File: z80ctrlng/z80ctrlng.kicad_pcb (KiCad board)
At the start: 2 copper layers, 99.8 x 49.9 mm, 46 parts, among them J1 BUS, J2 Micro_SD_Card_Det2, J3 UEXT, J4 SERIAL, J6 UPDI, Q1 BSS138, SW1 RESET, SW2 SW_DPDT_x2, SW3 SW_SP3T, SW4 SW_DIP_x06, SW5 SW_DPST, SW6 SW_DPST, U1 AVR128DB64x-xPT, U2 MIC5504-3.3YM5, U3 MCP7940N-xST, U5 74HCT574, U6 74HCT257, U7 AS6C4008-55PCN, Y1 32kHz

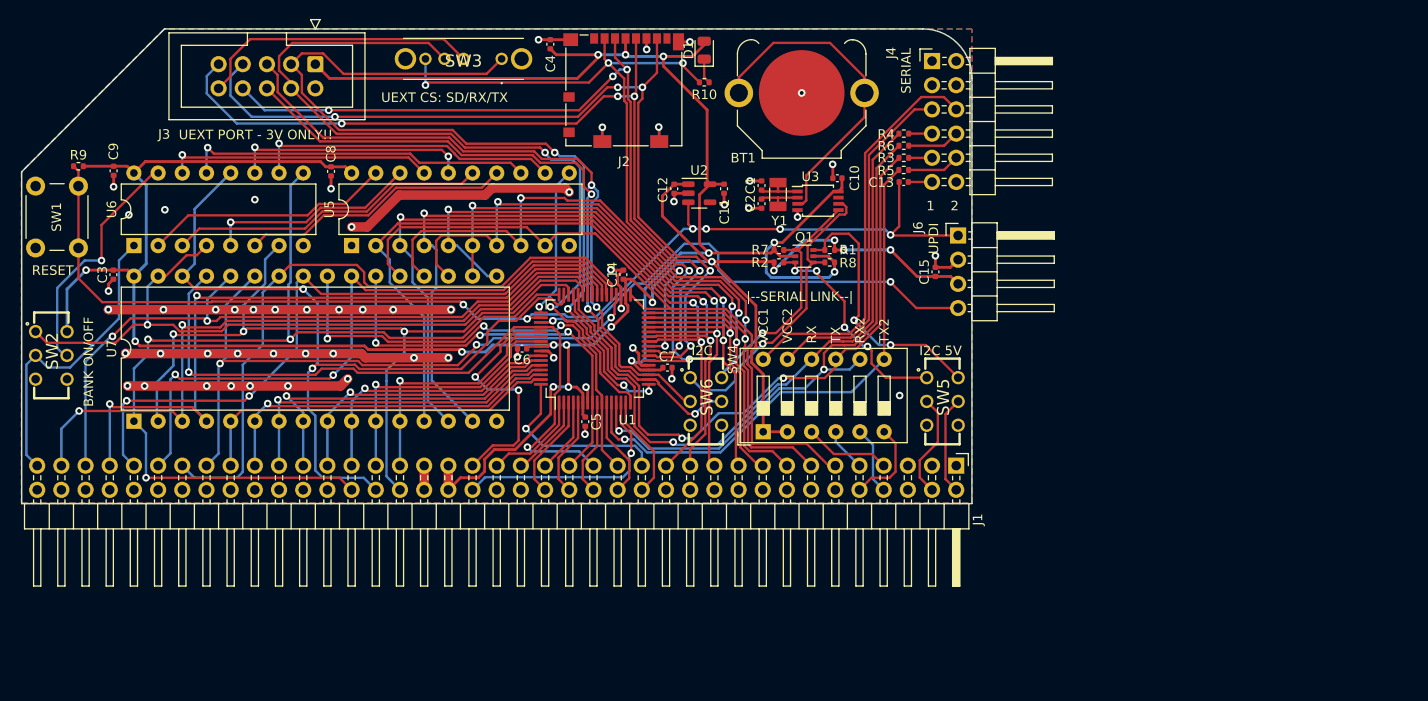
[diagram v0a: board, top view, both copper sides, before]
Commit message: Rework bus links using jumpers instead of dip switches; add labels
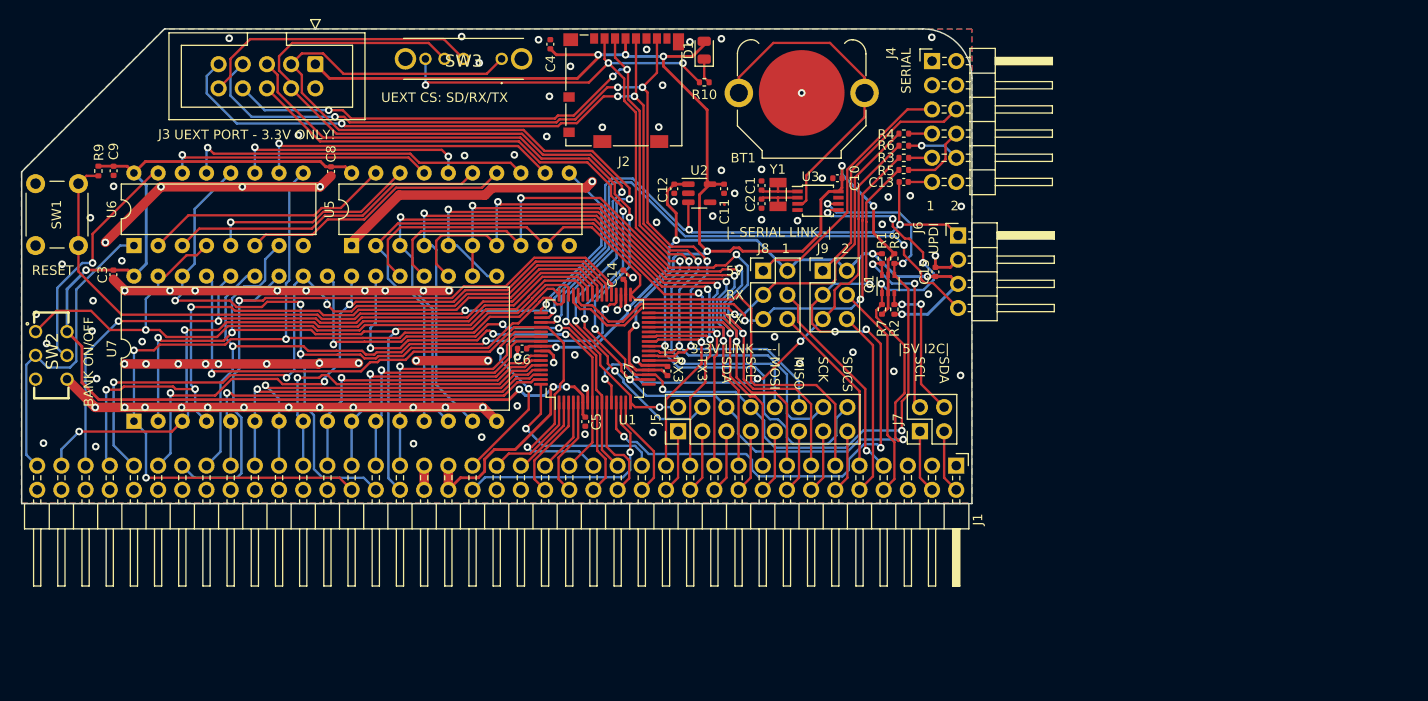
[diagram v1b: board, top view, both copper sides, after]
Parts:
- removed SW4: SW_DIP_x06, Button_Switch_THT:SW_DIP_SPSTx06_Slide_9.78x17.42mm_W7.62mm_P2.54mm
- removed SW5, SW6: SW_DPST, SamacSys_Parts:JS202011CQN
- added J5: 3V_LINK, Connector_PinHeader_2.54mm:PinHeader_2x08_P2.54mm_Vertical, F.Cu at (161.5, 100.5)
- added J7: I2C_LINK, Connector_PinHeader_2.54mm:PinHeader_2x02_P2.54mm_Vertical, F.Cu at (186.9, 100.5)
- added J8: S1_LINK, Connector_PinHeader_2.54mm:PinHeader_2x03_P2.54mm_Vertical, F.Cu at (170.5, 83.7)
- added J9: S2_LINK, Connector_PinHeader_2.54mm:PinHeader_2x03_P2.54mm_Vertical, F.Cu at (176.7, 83.7)
- moved R2 13.1 mm to (184.3, 87.7), turned to 90 degrees
- moved R7 12.5 mm to (183.0, 87.7), turned to 90 degrees
- moved Q1 9.27 mm to (183.6, 85.1), turned to 90 degrees
- moved R8 6.80 mm to (184.3, 82.4), turned to -90 degrees
- moved R1 5.56 mm to (183.0, 82.4), turned to -90 degrees
- moved R9 2.15 mm to (100.7, 73.2), turned to 90 degrees
- moved C7 0.36 mm to (160.4, 94.2), turned to 90 degrees
- moved SW1 0.25 mm to (94.1, 81.0)
- turned R6 to 180 degrees
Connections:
- J1 pad 43: +5V -> /5V
- J1 pad 44: +5V -> /5V
- Q1 pad 1: /SDA3V -> /SDA
- Q1 pad 3: /SCL5V -> /SDA5V
- Q1 pad 4: /SCL3V -> /SCL
- Q1 pad 6: /SDA5V -> /SCL5V
- R1 pad 2: /SDA5V -> /SCL5V
- R2 pad 2: /SCL5V -> /SDA5V
- R5 pad 1: /TX2 -> /RX2
- R5 pad 2: Net-(J4-Pin_10) -> Net-(J4-Pin_8)
- R6 pad 1: /RX2 -> Net-(J4-Pin_10)
- R6 pad 2: Net-(J4-Pin_8) -> /TX2
- R7 pad 2: /SDA3V -> /SDA
- R8 pad 2: /SCL3V -> /SCL
- U3 pad 5: /SDA3V -> /SDA
- U3 pad 6: /SCL3V -> /SCL
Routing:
- net /SDA: track 73.0 -> 142.3 mm, vias 3 -> 8
- net /SCL: track 71.4 -> 134.7 mm, vias 2 -> 6
- net /SCL3V: track 32.4 -> 0.00 mm, vias 1 -> 0
- net /~{SDCS}: track 71.9 -> 101.8 mm
- net GND: track 161.0 -> 187.9 mm, vias 57 -> 98
- net /SDA3V: track 25.6 -> 0.00 mm, vias 1 -> 0
- net /SCK: track 91.6 -> 113.0 mm
- net +5V: track 231.5 -> 212.3 mm, vias 14 -> 10
- net /RX: track 69.1 -> 50.0 mm
- net Net-(J4-Pin_6): track 42.4 -> 25.4 mm
- net /TX: track 66.6 -> 50.5 mm
- net /RX2: track 61.2 -> 77.2 mm, vias 2 -> 5
- net /BRX2: track 7.13 -> 23.0 mm
- net /MISO: track 93.0 -> 108.1 mm
- net /BTX: track 4.59 -> 18.5 mm
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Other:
- board text added: "512KB SRAM"
- board text added: "5V"
- board text added: "AVR128DB64"
- board text added: "BANK MULTIPLEXER"
- board text added: "BANK REGISTER"
- board text added: "GND"
- board text added: "MISO"
- board text added: "MOSI"
- board text added: "PA1"
- board text added: "PA2"
- board text added: "PA3"
- board text added: "PA4"
- board text added: "PA5^"
- board text added: "PA6"
- board text added: "PA7^"
- board text added: "PB0"
- board text added: "PB1^"
- board text added: "PB2"
- board text added: "PB3^"
- board text added: "PB4^"
- board text added: "PB5^"
- board text added: "PB6^"
- board text added: "PB7^"
- board text added: "PC0"
- board text added: "PC1"
- board text added: "PC2"
- board text added: "PC3"
- board text added: "PC4"
- board text added: "PC5"
- board text added: "PC6"
- board text added: "PC7"
- board text added: "PD0"
- board text added: "PD1"
- board text added: "PD2"
- board text added: "PD3"
- board text added: "PD4"
- board text added: "PD5"
- board text added: "PD6"
- board text added: "PD7"
- board text added: "PE0"
- board text added: "PE1"
- board text added: "PE2"
- board text added: "PE3"
- board text added: "PE4"
- board text added: "PE5"
- board text added: "PE6"
- board text added: "PE7"
- board text added: "PF0^"
- board text added: "PF1^"
- board text added: "PF2^"
- board text added: "PF3^"
- board text added: "PF4^"
- board text added: "PF5"
- board text added: "PG0"
- board text added: "PG1"
- board text added: "PG2"
- board text added: "PG3"
- board text added: "PG4"
- board text added: "PG5"
- board text added: "PG6"
- board text added: "PG7"
- board text added: "RX3"
- board text added: "SCK"
- board text added: "SCL"
- board text added: "SDA"
- board text added: "SDCS"
- board text added: "TX3"
- board text added: "UEXT PORT - 3.3V ONLY!"
- board text added: "|- SERIAL LINK -|"
- board text added: "|---- 3.3V LINK ----|"
- board text added: "|5V I2C|"
- board text removed: "I2C"
- board text removed: "I2C 5V"
- board text removed: "RX2"
- board text removed: "TX2"
- board text removed: "UEXT PORT - 3V ONLY!!"
- board text removed: "VCC1"
- board text removed: "VCC2"
- board text removed: "|--SERIAL LINK--|"

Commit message: More cleanup, fixing errors
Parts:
- added J10: QWIIC, Custom:JST_SM04B-SRSS-TB_LF__SN_, F.Cu at (97.6, 87.6)
- added R11: 100K, Resistor_SMD:R_0402_1005Metric, F.Cu at (147.4, 62.4)
- added R12: 100K, Resistor_SMD:R_0402_1005Metric, F.Cu at (147.4, 65.4)
- added R13: 100K, Resistor_SMD:R_0402_1005Metric, F.Cu at (147.4, 63.9)
- added R14: 100K, Resistor_SMD:R_0402_1005Metric, F.Cu at (147.4, 60.9)
- added SW4: RTC, Custom:SWITCH_011CQN, F.Cu at (182.8, 94.8)
- J2: value Micro_SD_Card_Det2 -> MICRO_SD
- J7: value I2C_LINK -> UEXT_CS; footprint Connector_PinHeader_2.54mm:PinHeader_2x02_P2.54mm_Vertical -> Connector_PinHeader_2.54mm:PinHeader_2x05_P2.54mm_Vertical
- SW2: value SW_DPDT_x2 -> BANK_EN; footprint SamacSys_Parts:JS202011CQN -> Custom:SWITCH_011CQN
- SW3: value SW_SP3T -> RTC; footprint SamacSys_Parts:OS103011MS8QP1 -> Custom:SWITCH_011CQN
- moved J7 65.8 mm to (131.9, 64.5)
- moved SW3 59.5 mm to (188.3, 94.8), turned to 0 degrees
- moved R1 7.31 mm to (188.1, 87.6), turned to 0 degrees
- moved R8 6.53 mm to (183.7, 88.9), turned to 0 degrees
- moved R2 4.01 mm to (188.1, 88.9), turned to 0 degrees
- moved SW2 2.92 mm to (94.1, 95.0), turned to 0 degrees
- moved R10 0.99 mm to (164.3, 62.9)
- moved C4 0.85 mm to (147.4, 59.4), turned to 0 degrees
- moved R7 0.80 mm to (183.7, 87.6), turned to 0 degrees
- moved Q1 0.52 mm to (183.7, 84.6), turned to 0 degrees
- moved C7 0.38 mm to (160.1, 94.1)
- moved C6 0.27 mm to (145.1, 91.6)
- moved C5 0.25 mm to (151.5, 99.5)
- turned C15 to -90 degrees
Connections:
- net /CLK renamed /Z80CLK
- J1 pad 43: /5V -> +5V
- J1 pad 44: /5V -> +5V
- J3 pad 10: Net-(J3-Pin_10) -> /~{UXCS}
- J4 pad 5: Net-(J4-Pin_5) -> /5VS1
- J4 pad 6: Net-(J4-Pin_6) -> /5VS2
- J6 pad 2: GND -> +5V
- J6 pad 3: +5V -> GND
- J7 pad 1: /USER6 -> /TX3
- J7 pad 2: /SCL5V -> /~{UXCS}
- J7 pad 3: /USER7 -> /RX3
- J7 pad 4: /SDA5V -> /~{UXCS}
- J8 pad 1: Net-(J4-Pin_5) -> +5V
- J8 pad 2: +5V -> /5VS1
- J9 pad 1: Net-(J4-Pin_6) -> +5V
- J9 pad 2: +5V -> /5VS2
- Q1 pad 3: /SDA5V -> /SCL5V
- Q1 pad 6: /SCL5V -> /SDA5V
- R1 pad 2: /SCL5V -> /SDA5V
- R2 pad 2: /SDA5V -> /SCL5V
- R7 pad 2: /SDA -> /SCL
- R8 pad 2: /SCL -> /SDA
- SW2 pad 4: +5V -> GND
- SW2 pad 6: GND -> +5V
- SW3 pad 1: /TX3 -> /USER6
- SW3 pad 2: Net-(J3-Pin_10) -> /USER7
- SW3 pad 3: /RX3 -> unconnected-(SW3-Pad3)
- SW3 pad 4: /~{SDCS} -> unconnected-(SW3-Pad4)
- SW3 pad 5: unconnected-(SW3-Pad5) -> /SDA5V
- SW3 pad 6: unconnected-(SW3-5-Pad6) -> /SCL5V
- U3 pad 5: /SDA -> Net-(U3-SDA)
- U3 pad 6: /SCL -> Net-(U3-SCL)
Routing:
- net +3.3V: track 137.0 -> 196.1 mm, vias 7 -> 12
- net /~{UXCS}: track 0.00 -> 47.0 mm, vias 0 -> 1
- net GND: track 187.9 -> 234.9 mm, vias 98 -> 68
- net Net-(J3-Pin_10): track 29.8 -> 0.00 mm
- net Net-(J4-Pin_5): track 27.4 -> 0.00 mm
- net Net-(U3-SDA): track 0.00 -> 27.3 mm, vias 0 -> 2
- net Net-(U3-SCL): track 0.00 -> 27.0 mm, vias 0 -> 3
- net /5VS1: track 0.00 -> 26.0 mm
- net Net-(J4-Pin_6): track 25.4 -> 0.00 mm
- net /SCL: track 134.7 -> 159.6 mm
- net /5VS2: track 0.00 -> 24.7 mm
- net /SDA: track 142.3 -> 164.5 mm, vias 8 -> 5
- net /TX3: track 101.9 -> 80.1 mm
- net /RX3: track 94.8 -> 73.8 mm, vias 3 -> 4
- net /~{SDCS}: track 101.8 -> 90.9 mm, vias 5 -> 4
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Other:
- board text added: "3.3V"
- board text added: "BANK ENABLE"
- board text added: "BUS"
- board text added: "PA0"
- board text added: "PF2"
- board text added: "PF3"
- board text added: "PF4"
- board text added: "QWIIC"
- board text added: "RTC"
- board text added: "UEXT CS PIN"
- board text added: "|-- I2C --|"
- board text removed: "BANK ON/OFF"
- board text removed: "UEXT CS: SD/RX/TX"
- board text removed: "|5V I2C|"

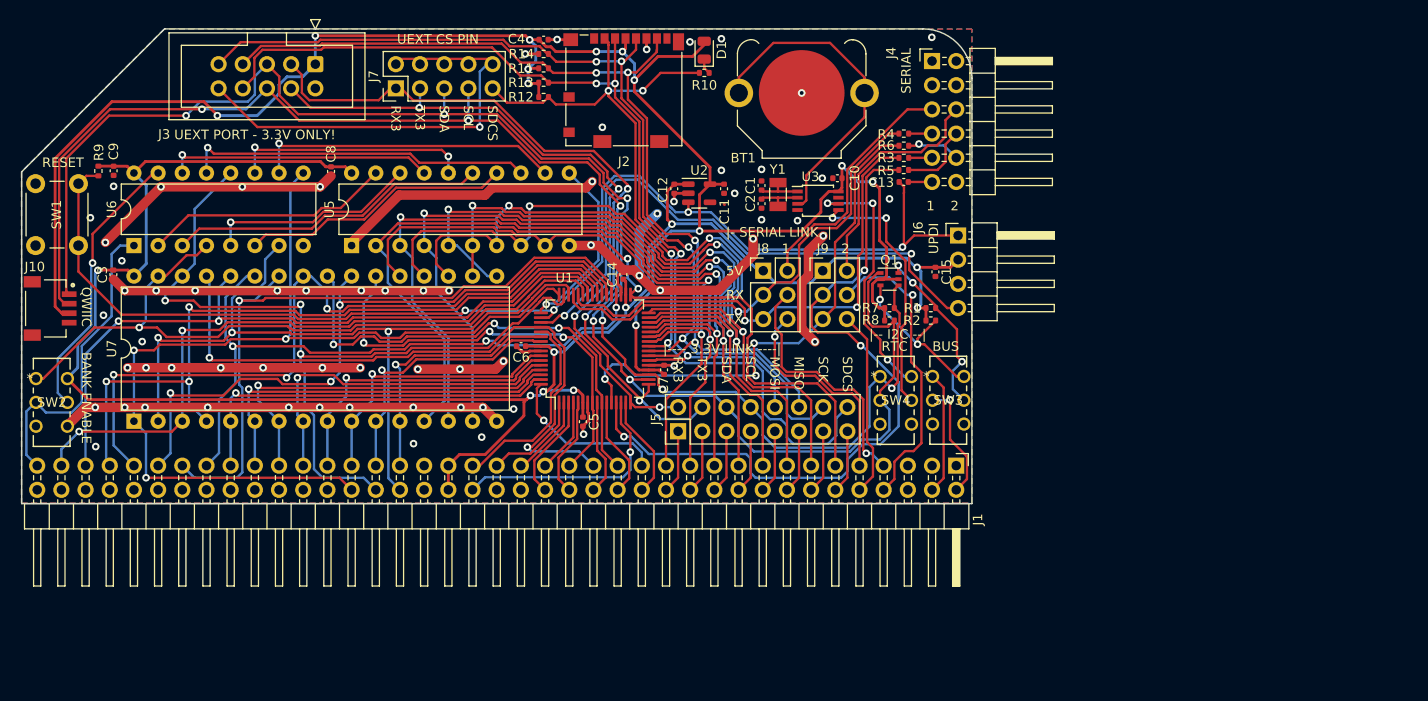
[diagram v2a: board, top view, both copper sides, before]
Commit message: Rework to make room for clock jumper
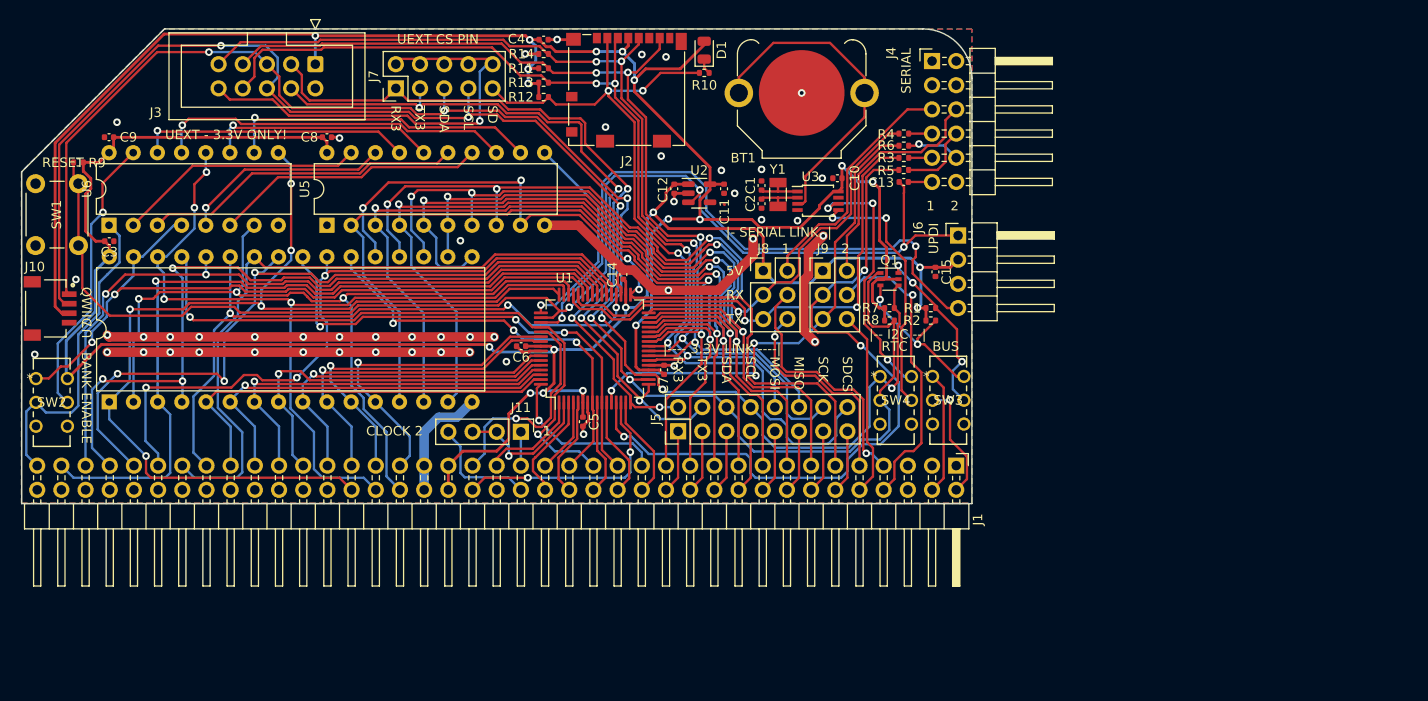
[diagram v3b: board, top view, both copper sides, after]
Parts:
- added J11: CLOCK, Connector_PinHeader_2.54mm:PinHeader_1x04_P2.54mm_Vertical, F.Cu at (145.0, 100.6)
- moved C8 3.61 mm to (124.7, 69.6), turned to 0 degrees
- moved C9 3.56 mm to (101.8, 69.6), turned to 180 degrees
- moved C3 3.54 mm to (101.8, 80.6), turned to 0 degrees
- moved U6 3.38 mm to (101.8, 78.9)
- moved U5 3.36 mm to (124.7, 78.9)
- moved U7 3.29 mm to (101.8, 97.4)
- moved R9 2.28 mm to (98.6, 72.3), turned to 0 degrees
- moved J2 0.29 mm to (156.1, 64.7)
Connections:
- J1 pad 37: /Z80CLK -> /CLOCK1
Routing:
- net GND: track 234.9 -> 150.9 mm, vias 68 -> 49
- net /CLOCK2: track 0.00 -> 11.7 mm
- net /D7: track 74.7 -> 84.4 mm, vias 2 -> 4
- net /A14: track 71.7 -> 81.3 mm, vias 2 -> 1
- net +5V: track 210.0 -> 218.1 mm
- net /SDA: track 164.5 -> 172.2 mm
- net /A1: track 28.8 -> 35.9 mm
- net /A0: track 27.3 -> 34.1 mm
- net /Z80CLK: track 8.67 -> 14.7 mm, vias 0 -> 1
- net /D5: track 81.8 -> 87.6 mm, vias 3 -> 4
- net /~{RESET}: track 131.3 -> 137.0 mm, vias 4 -> 3
- net /A2: track 29.4 -> 35.1 mm
- net /D6: track 87.3 -> 92.7 mm, vias 3 -> 4
- net /D3: track 75.3 -> 80.0 mm
- net /A16: track 85.0 -> 89.6 mm
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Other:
- board text added: "3V3"
- board text added: "CLOCK 2"
- board text added: "SD"
- board text added: "UEXT - 3.3V ONLY!"
- board text removed: "3.3V"
- board text removed: "UEXT PORT - 3.3V ONLY!"
